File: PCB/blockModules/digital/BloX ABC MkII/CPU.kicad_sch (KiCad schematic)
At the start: 11 parts, among them U201 HEADER_3x2, U202 ATmega328-A, Y201 Crystal_GND2

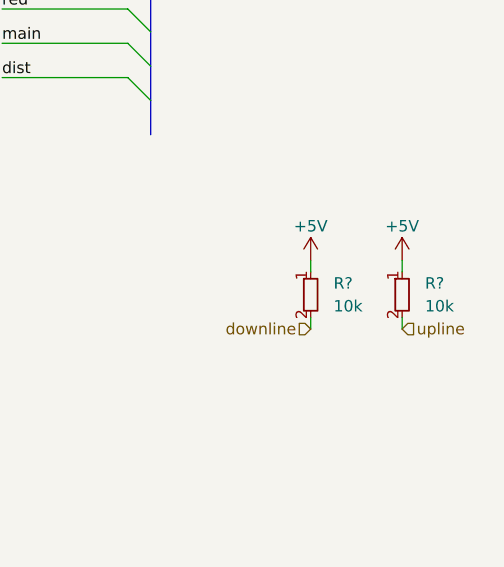
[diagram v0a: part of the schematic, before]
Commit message: added servo driver and S88 image
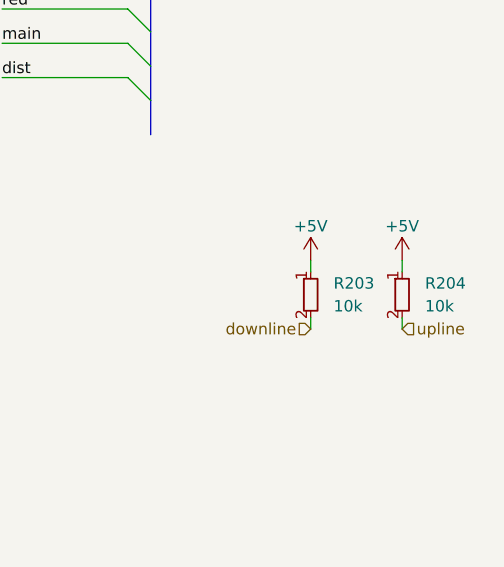
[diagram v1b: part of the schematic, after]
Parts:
- gave numbers to parts that had none: 2
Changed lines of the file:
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@@
   (symbol (lib_id "power:+5V") (at 251.46 66.04 0) (unit 1)
     (in_bom yes) (on_board yes) (dnp no)
-    (property "Reference" "#PWR0113" (at 251.46 69.85 0)
+    (property "Reference" "#PWR0204" (at 251.46 69.85 0)
       (effects (font (size 1.27 1.27)) hide)
     )
@@
     (instances
       (project "BloX_ABC_MkII"
-        (path "/8a26887a-4615-4d87-8c0a-2e69eaebfe7b"
-          (reference "#PWR0113") (unit 1)
-        )
         (path "/8a26887a-4615-4d87-8c0a-2e69eaebfe7b/88ae271b-145e-4e05-8f06-1bced5dafa44"
           (reference "#PWR0204") (unit 1)
@@
   (symbol (lib_id "power:+5V") (at 241.3 66.04 0) (unit 1)
     (in_bom yes) (on_board yes) (dnp no)
-    (property "Reference" "#PWR0113" (at 241.3 69.85 0)
+    (property "Reference" "#PWR0203" (at 241.3 69.85 0)
       (effects (font (size 1.27 1.27)) hide)
     )
@@
     (instances
       (project "BloX_ABC_MkII"
-        (path "/8a26887a-4615-4d87-8c0a-2e69eaebfe7b"
-          (reference "#PWR0113") (unit 1)
-        )
         (path "/8a26887a-4615-4d87-8c0a-2e69eaebfe7b/88ae271b-145e-4e05-8f06-1bced5dafa44"
           (reference "#PWR0203") (unit 1)
@@
   (symbol (lib_id "resistors_0603:R_10k_0603") (at 251.46 69.85 0) (unit 1)
     (in_bom yes) (on_board yes) (dnp no) (fields_autoplaced)
-    (property "Reference" "R?" (at 254 68.58 0)
+    (property "Reference" "R204" (at 254 68.58 0)
       (effects (font (size 1.27 1.27)) (justify left))
     )
@@
     (instances
       (project "BloX_ABC_MkII"
-        (path "/8a26887a-4615-4d87-8c0a-2e69eaebfe7b"
-          (reference "R?") (unit 1)
-        )
         (path "/8a26887a-4615-4d87-8c0a-2e69eaebfe7b/88ae271b-145e-4e05-8f06-1bced5dafa44"
           (reference "R204") (unit 1)
@@
   (symbol (lib_id "resistors_0603:R_10k_0603") (at 241.3 69.85 0) (unit 1)
     (in_bom yes) (on_board yes) (dnp no) (fields_autoplaced)
-    (property "Reference" "R?" (at 243.84 68.58 0)
+    (property "Reference" "R203" (at 243.84 68.58 0)
       (effects (font (size 1.27 1.27)) (justify left))
     )
@@
     (instances
       (project "BloX_ABC_MkII"
-        (path "/8a26887a-4615-4d87-8c0a-2e69eaebfe7b"
-          (reference "R?") (unit 1)
-        )
         (path "/8a26887a-4615-4d87-8c0a-2e69eaebfe7b/88ae271b-145e-4e05-8f06-1bced5dafa44"
           (reference "R203") (unit 1)
